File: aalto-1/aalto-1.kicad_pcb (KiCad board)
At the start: 2 copper layers, 1 part

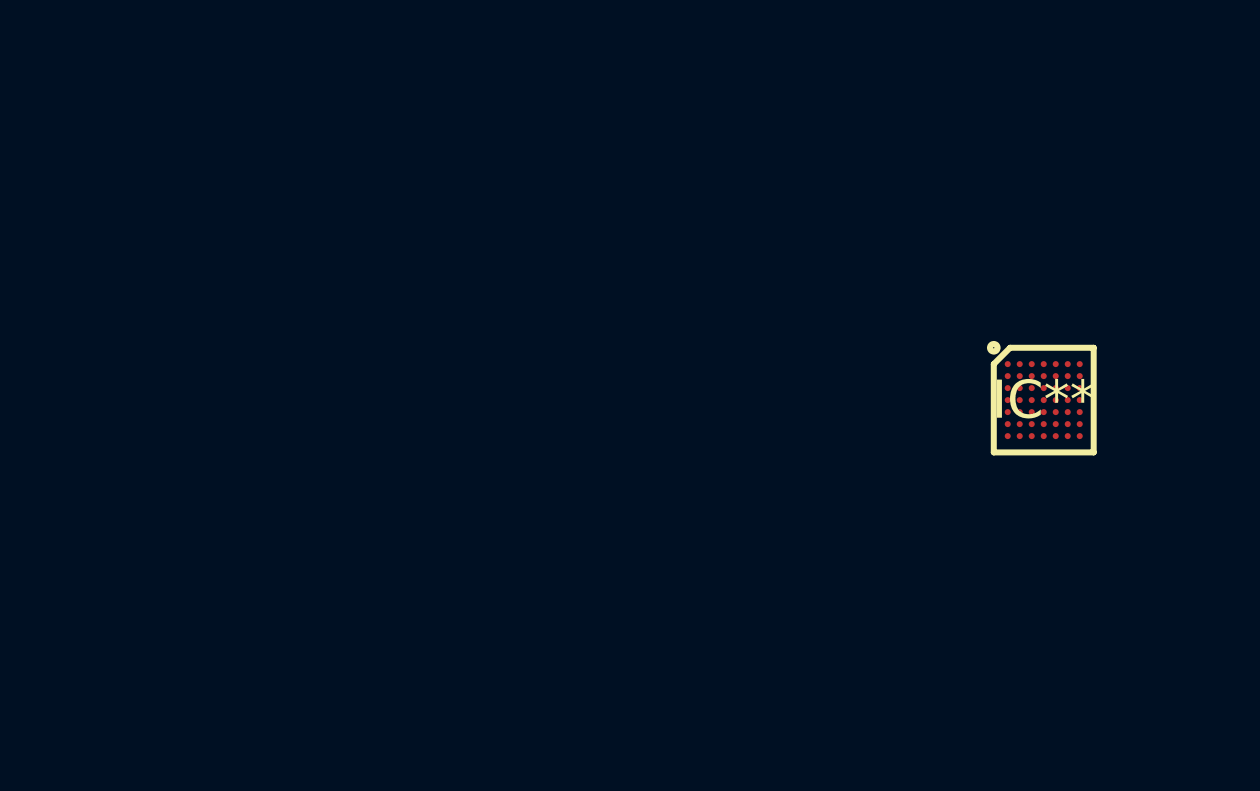
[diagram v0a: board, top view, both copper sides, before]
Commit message: added footprints
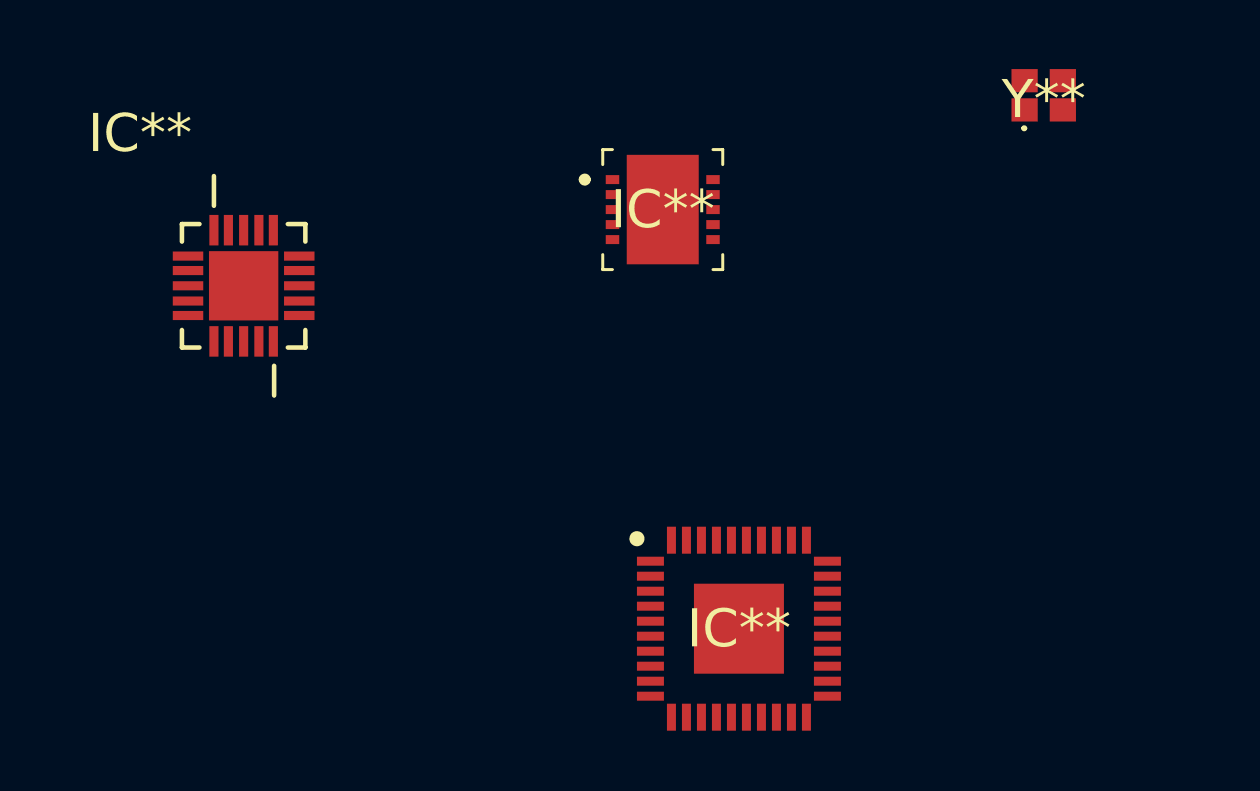
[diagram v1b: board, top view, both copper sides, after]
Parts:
- removed the IC** at (222.2, 62.2)
- added IC**: RFPA5200, RFPA5200:RFPA5200, F.Cu at (209.6, 55.9)
- added IC**: QFN50P600X600X100-41N-D, MSP430F2274IRHAT:QFN50P600X600X100-41N-D, F.Cu at (212.1, 69.8)
- added IC**: QFN50P400X400X90-21N, CC2500-RTY1:QFN50P400X400X90-21N, F.Cu at (195.6, 58.4)
- added Y**: ABM11W300000MHZ4B1UT3, ABM11W-26.0000MHZ-6-D1X-T3:ABM11W300000MHZ4B1UT3, F.Cu at (222.2, 52.1)

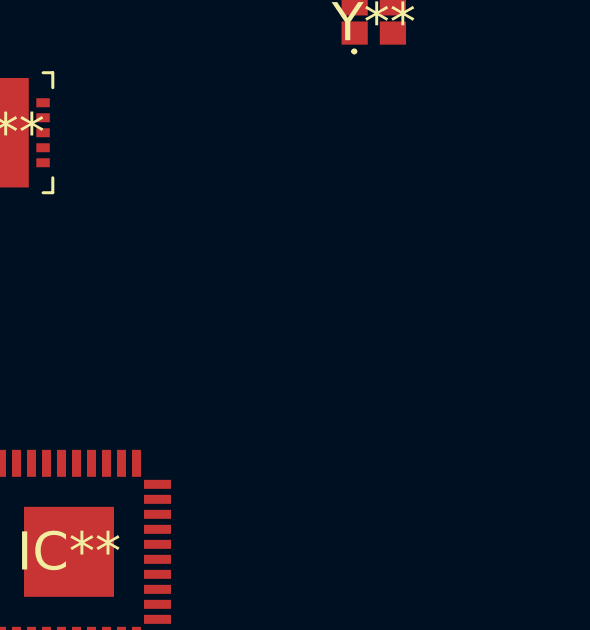
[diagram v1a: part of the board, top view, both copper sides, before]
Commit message: power switch footprint
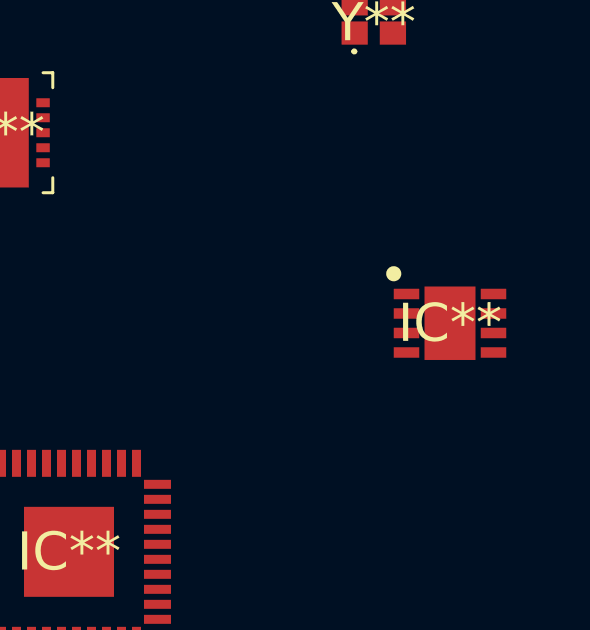
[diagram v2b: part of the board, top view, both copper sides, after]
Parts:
- added IC**: SON65P300X300X100-9N-D, TPS2556QDRBRQ1:SON65P300X300X100-9N-D, F.Cu at (224.8, 62.2)
